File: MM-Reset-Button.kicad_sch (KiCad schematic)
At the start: 2 parts, among them SW2 Switch

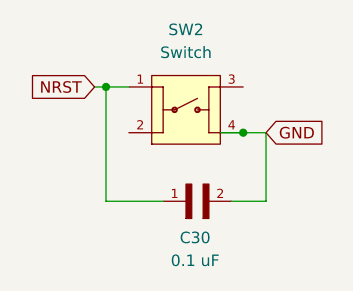
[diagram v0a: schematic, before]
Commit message: added power switch
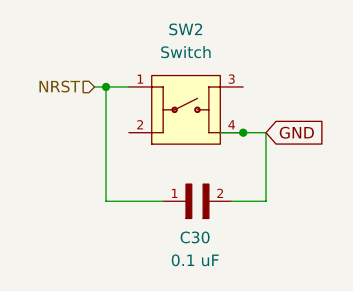
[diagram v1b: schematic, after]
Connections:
- net NRST renamed  NRST
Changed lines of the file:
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@@
 		)
 	)
-	(global_label "NRST"
+	(hierarchical_label " NRST"
 		(shape input)
 		(at 82.55 62.23 180)
-		(fields_autoplaced yes)
 		(effects
 			(font
@@
 			(justify right)
 		)
-		(property "Intersheetrefs" "${INTERSHEET_REFS}"
-			(at 74.7872 62.23 0)
-			(effects
-				(font
-					(size 1.27 1.27)
-				)
-				(justify right)
-				(hide yes)
-			)
-		)
 	)

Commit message: fixedled orignetation and linked to ground + duplicated IR emitter/receiver pairs
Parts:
- C30: footprint 0.1µFCapacitor_footprints:CAP_0402_N_WAL-L -> Ceramic_Capacitor_0.1uF_CL21B104KBCNNNC:CAPC2012X95N
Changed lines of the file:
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@@
 			)
 		)
-		(property "Footprint" "0.1µFCapacitor_footprints:CAP_0402_N_WAL-L"
+		(property "Footprint" "Ceramic_Capacitor_0.1uF_CL21B104KBCNNNC:CAPC2012X95N"
 			(at 92.71 74.93 0)
 			(effects

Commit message: Add files via upload
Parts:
- removed C30: 0.1 uF, Ceramic_Capacitor_0.1uF_CL21B104KBCNNNC:CAPC2012X95N, symbol 10uF_Capacitor_GRM188R61C106MAALD:GRM188R61C106MAALD
- added C7: 0.1 µF, CL05A104KA5NNNC:CAPC1005X55N, symbol 0.1µFCapacitor_CL05A104KA5NNNC:CL05A104KA5NNNC
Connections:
- net  NRST: now also C7.1
- net GND: now also C7.2
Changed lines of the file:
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@@
 	)
 	(symbol
-		(lib_id "10uF_Capacitor_GRM188R61C106MAALD:GRM188R61C106MAALD")
+		(lib_id "0.1µFCapacitor_CL05A104KA5NNNC:CL05A104KA5NNNC")
 		(at 92.71 74.93 0)
 		(unit 1)
@@
 		(on_board yes)
 		(dnp no)
-		(property "Reference" "C30"
-			(at 93.726 78.994 0)
-			(effects
-				(font
-					(size 1.27 1.27)
-				)
-			)
-		)
-		(property "Value" "0.1 uF"
-			(at 93.726 81.534 0)
-			(effects
-				(font
-					(size 1.27 1.27)
-				)
-			)
-		)
-		(property "Footprint" "Ceramic_Capacitor_0.1uF_CL21B104KBCNNNC:CAPC2012X95N"
+		(fields_autoplaced yes)
+		(property "Reference" "C7"
+			(at 93.98 68.58 0)
+			(effects
+				(font
+					(size 1.27 1.27)
+				)
+			)
+		)
+		(property "Value" "0.1 µF"
+			(at 93.98 71.12 0)
+			(effects
+				(font
+					(size 1.27 1.27)
+				)
+			)
+		)
+		(property "Footprint" "CL05A104KA5NNNC:CAPC1005X55N"
 			(at 92.71 74.93 0)
 			(effects
@@
 			)
 		)
+		(property "E_max" "0.55"
+			(at 92.71 74.93 0)
+			(effects
+				(font
+					(size 1.27 1.27)
+				)
+				(justify bottom)
+				(hide yes)
+			)
+		)
+		(property "L_max" "0.35"
+			(at 92.71 74.93 0)
+			(effects
+				(font
+					(size 1.27 1.27)
+				)
+				(justify bottom)
+				(hide yes)
+			)
+		)
+		(property "A_max" "0.55"
+			(at 92.71 74.93 0)
+			(effects
+				(font
+					(size 1.27 1.27)
+				)
+				(justify bottom)
+				(hide yes)
+			)
+		)
+		(property "L1_nom" "0.25"
+			(at 92.71 74.93 0)
+			(effects
+				(font
+					(size 1.27 1.27)
+				)
+				(justify bottom)
+				(hide yes)
+			)
+		)
+		(property "D_max" "1.05"
+			(at 92.71 74.93 0)
+			(effects
+				(font
+					(size 1.27 1.27)
+				)
+				(justify bottom)
+				(hide yes)
+			)
+		)
+		(property "A_nom" "0.55"
+			(at 92.71 74.93 0)
+			(effects
+				(font
+					(size 1.27 1.27)
+				)
+				(justify bottom)
+				(hide yes)
+			)
+		)
+		(property "L1_max" "0.35"
+			(at 92.71 74.93 0)
+			(effects
+				(font
+					(size 1.27 1.27)
+				)
+				(justify bottom)
+				(hide yes)
+			)
+		)
+		(property "L1_min" "0.15"
+			(at 92.71 74.93 0)
+			(effects
+				(font
+					(size 1.27 1.27)
+				)
+				(justify bottom)
+				(hide yes)
+			)
+		)
+		(property "A_min" "0.55"
+			(at 92.71 74.93 0)
+			(effects
+				(font
+					(size 1.27 1.27)
+				)
+				(justify bottom)
+				(hide yes)
+			)
+		)
+		(property "E_min" "0.45"
+			(at 92.71 74.93 0)
+			(effects
+				(font
+					(size 1.27 1.27)
+				)
+				(justify bottom)
+				(hide yes)
+			)
+		)
+		(property "D_min" "0.95"
+			(at 92.71 74.93 0)
+			(effects
+				(font
+					(size 1.27 1.27)
+				)
+				(justify bottom)
+				(hide yes)
+			)
+		)
+		(property "D_nom" "1.0"
+			(at 92.71 74.93 0)
+			(effects
+				(font
+					(size 1.27 1.27)
+				)
+				(justify bottom)
+				(hide yes)
+			)
+		)
+		(property "E_nom" "0.5"
+			(at 92.71 74.93 0)
+			(effects
+				(font
+					(size 1.27 1.27)
+				)
+				(justify bottom)
+				(hide yes)
+			)
+		)
+		(property "STANDARD" "IPC 7351B"
+			(at 92.71 74.93 0)
+			(effects
+				(font
+					(size 1.27 1.27)
+				)
+				(justify bottom)
+				(hide yes)
+			)
+		)
+		(property "L_min" "0.15"
+			(at 92.71 74.93 0)
+			(effects
+				(font
+					(size 1.27 1.27)
+				)
+				(justify bottom)
+				(hide yes)
+			)
+		)
+		(property "L_nom" "0.25"
+			(at 92.71 74.93 0)
+			(effects
+				(font
+					(size 1.27 1.27)
+				)
+				(justify bottom)
+				(hide yes)
+			)
+		)
+		(property "MANUFACTURER" "Samsung Electro-Mechanics"
+			(at 92.71 74.93 0)
+			(effects
+				(font
+					(size 1.27 1.27)
+				)
+				(justify bottom)
+				(hide yes)
+			)
+		)
+		(pin "2"
+		)
 		(pin "1"
-		)
-		(pin "2"
 		)
 		(instances
 			(project "IREmitter"
 				(path "/d311851a-8b0b-4acf-b2e7-1b968b2adbe7/084a0d9c-4e38-4ee1-a3cf-a1ffe53c2804"
-					(reference "C30")
+					(reference "C7")
 					(unit 1)
 				)

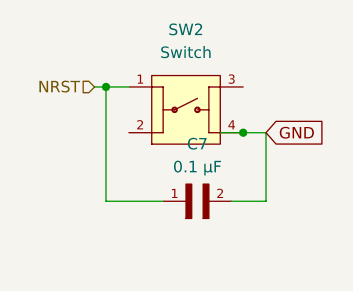
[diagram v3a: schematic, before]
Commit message: redid the 4 emitters receivers, fixed orientation of LEDS and going to continue adding footprints and replace the 60ohm resistors with 300ohm ones
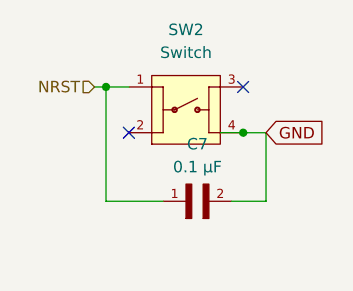
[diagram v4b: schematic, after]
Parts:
- C7: footprint CL05A104KA5NNNC:CAPC1005X55N -> Ceramic_Capacitor_0.1uF_CL21B104KBCNNNC:CAPC2012X95N
- SW2: footprint Switch_FSM4JSMATR_footprint:SW_4-1437565-2 -> Switch_4-1437565-2:SW_4-1437565-2
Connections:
- no-connect marks 0 -> 2
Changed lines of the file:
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@@
 		(color 0 0 0 0)
+	)
+	(no_connect
+		(at 99.06 62.23)
+	)
+	(no_connect
+		(at 86.36 67.31)
 	)
 	(wire
@@
 			)
 		)
-		(property "Footprint" "CL05A104KA5NNNC:CAPC1005X55N"
+		(property "Footprint" "Ceramic_Capacitor_0.1uF_CL21B104KBCNNNC:CAPC2012X95N"
 			(at 92.71 74.93 0)
 			(effects
@@
 			)
 		)
-		(property "Footprint" "Switch_FSM4JSMATR_footprint:SW_4-1437565-2"
+		(property "Footprint" "Switch_4-1437565-2:SW_4-1437565-2"
 			(at 92.71 64.77 0)
 			(effects
